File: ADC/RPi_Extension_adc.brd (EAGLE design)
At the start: 63 x 50 mm, 47 parts, among them U1 74AHC1G04GW/T1, U2 ADR423ARZ, U3 AD7616BSTZ

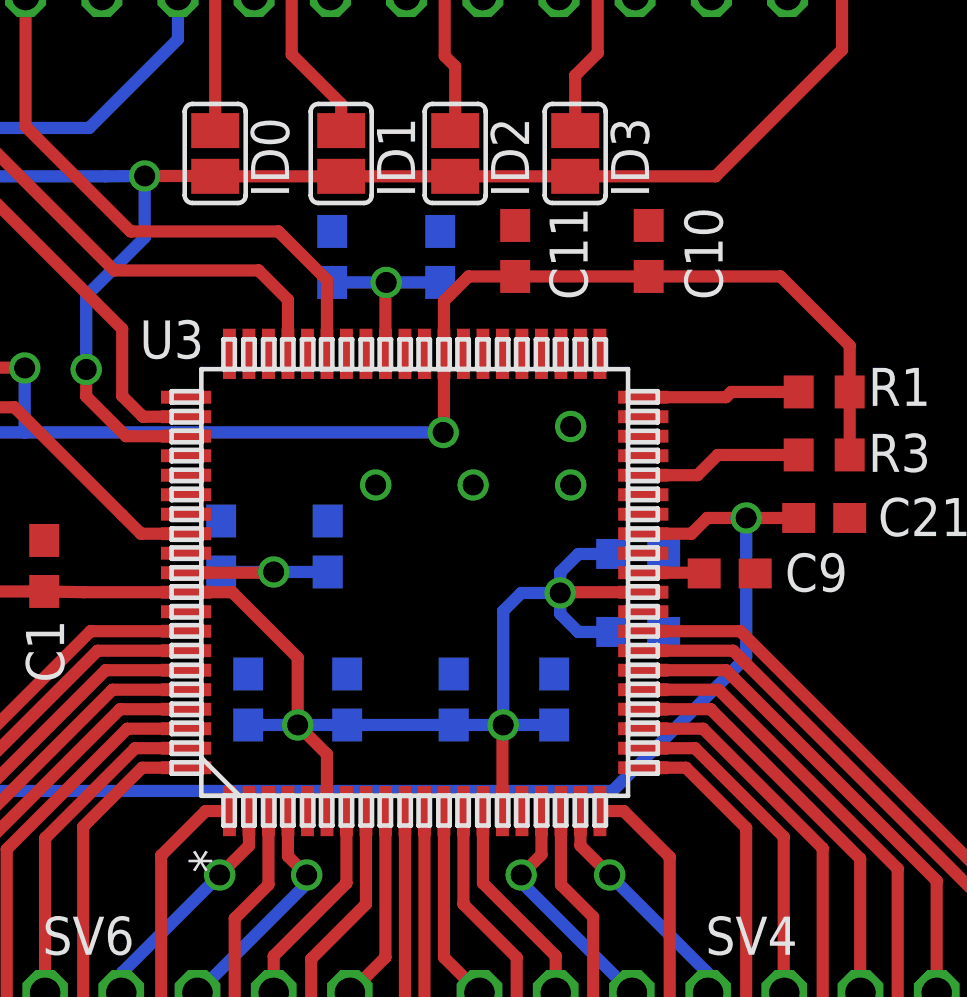
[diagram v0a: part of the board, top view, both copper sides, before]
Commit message: small relocations of decoupling caps on adc board
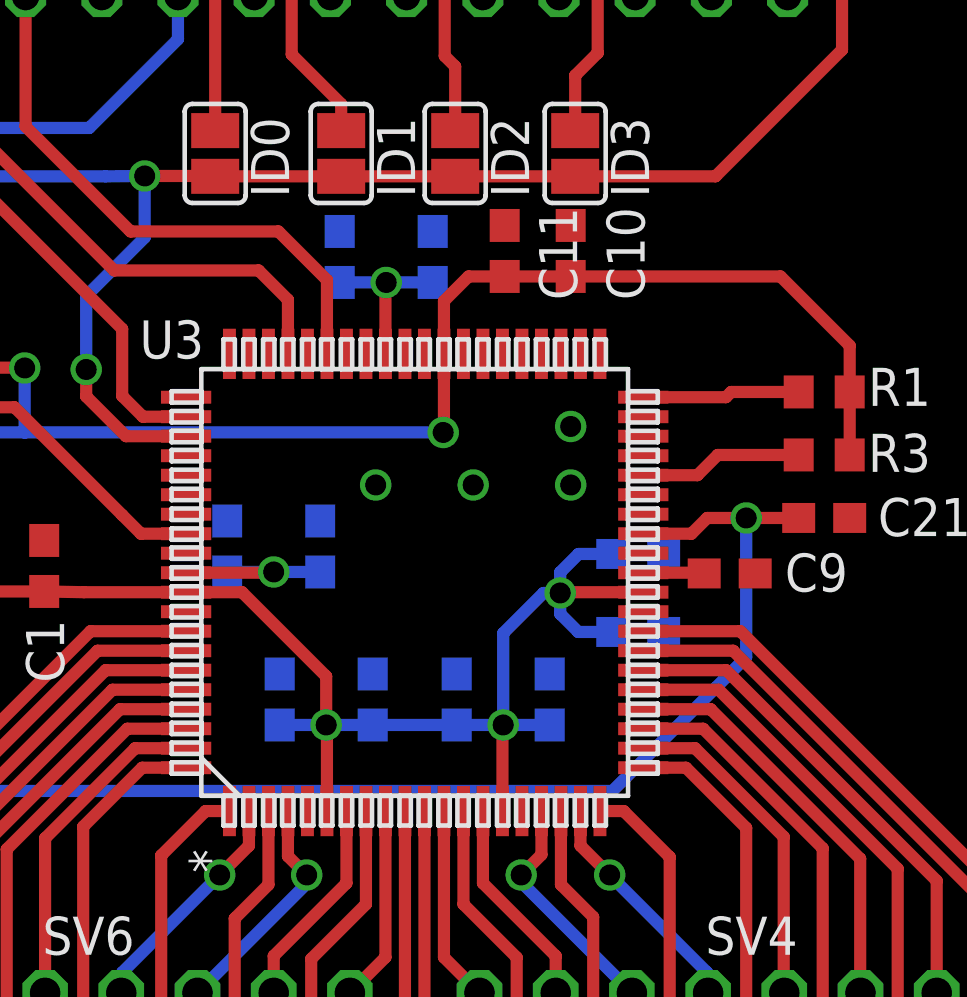
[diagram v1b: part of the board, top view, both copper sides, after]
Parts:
- moved C10 2.60 mm to (45.5, 31.9)
- moved C4 1.05 mm to (35.8, 16.9)
- moved C3 0.85 mm to (38.9, 16.9)
- moved C11 0.35 mm to (43.3, 31.9)
- moved C18 0.25 mm to (37.1, 22.0)
- moved C19 0.25 mm to (37.8, 31.6)
- moved C20 0.25 mm to (40.9, 31.6)
- moved C12 0.20 mm to (34.0, 22.0)
- moved C6 0.15 mm to (44.8, 16.9)
- moved C5 0.10 mm to (41.7, 16.9)
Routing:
- net +5V: track 86.0 -> 84.6 mm
- net N$16: track 5.99 -> 5.49 mm
